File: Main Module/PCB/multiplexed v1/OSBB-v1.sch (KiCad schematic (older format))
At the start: 30 parts, among them P1 AUX 1, P10 +3.3V Pins, P11 BTN-1-4, P12 BTN-5-8, P13 BTN-9-12, P14 EXTRA Pins, P15 BTN-17-20, P16 BTN-13-16, P17 BTN-25-28, P18 BTN-21-24, P19 BTN-29-32, P2 AUX 2, P3 AUX 3, P4 Pit limiter, P5 Rotary Encoders, P6 GND Pins, Q1 Q_NPN_CBE, Q2 Q_NPN_CBE, Q3 Q_NPN_CBE, U1 74HC4051, U2 74HC4051, U3 74HC4051, U4 74HC4051, U5 Teensy3.2

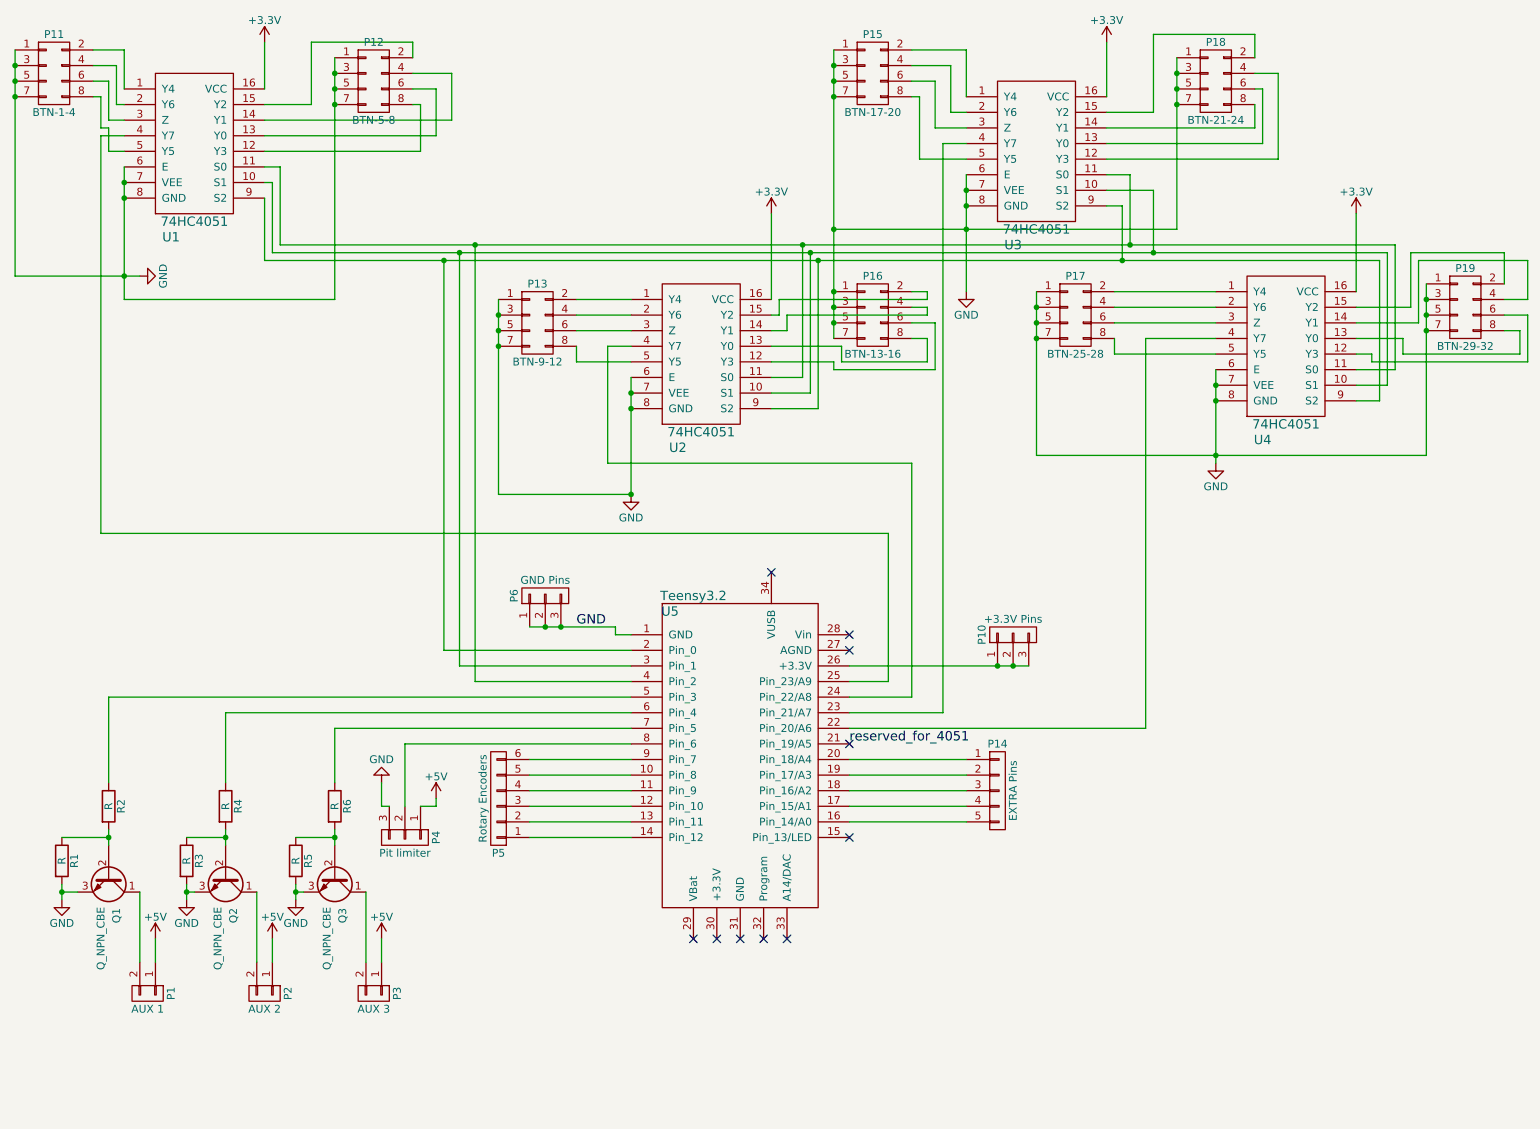
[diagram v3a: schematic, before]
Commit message: * updated schematic to use 2x32 pin header to make it easier to connect PCB * PCB is connected, still needs to be checked
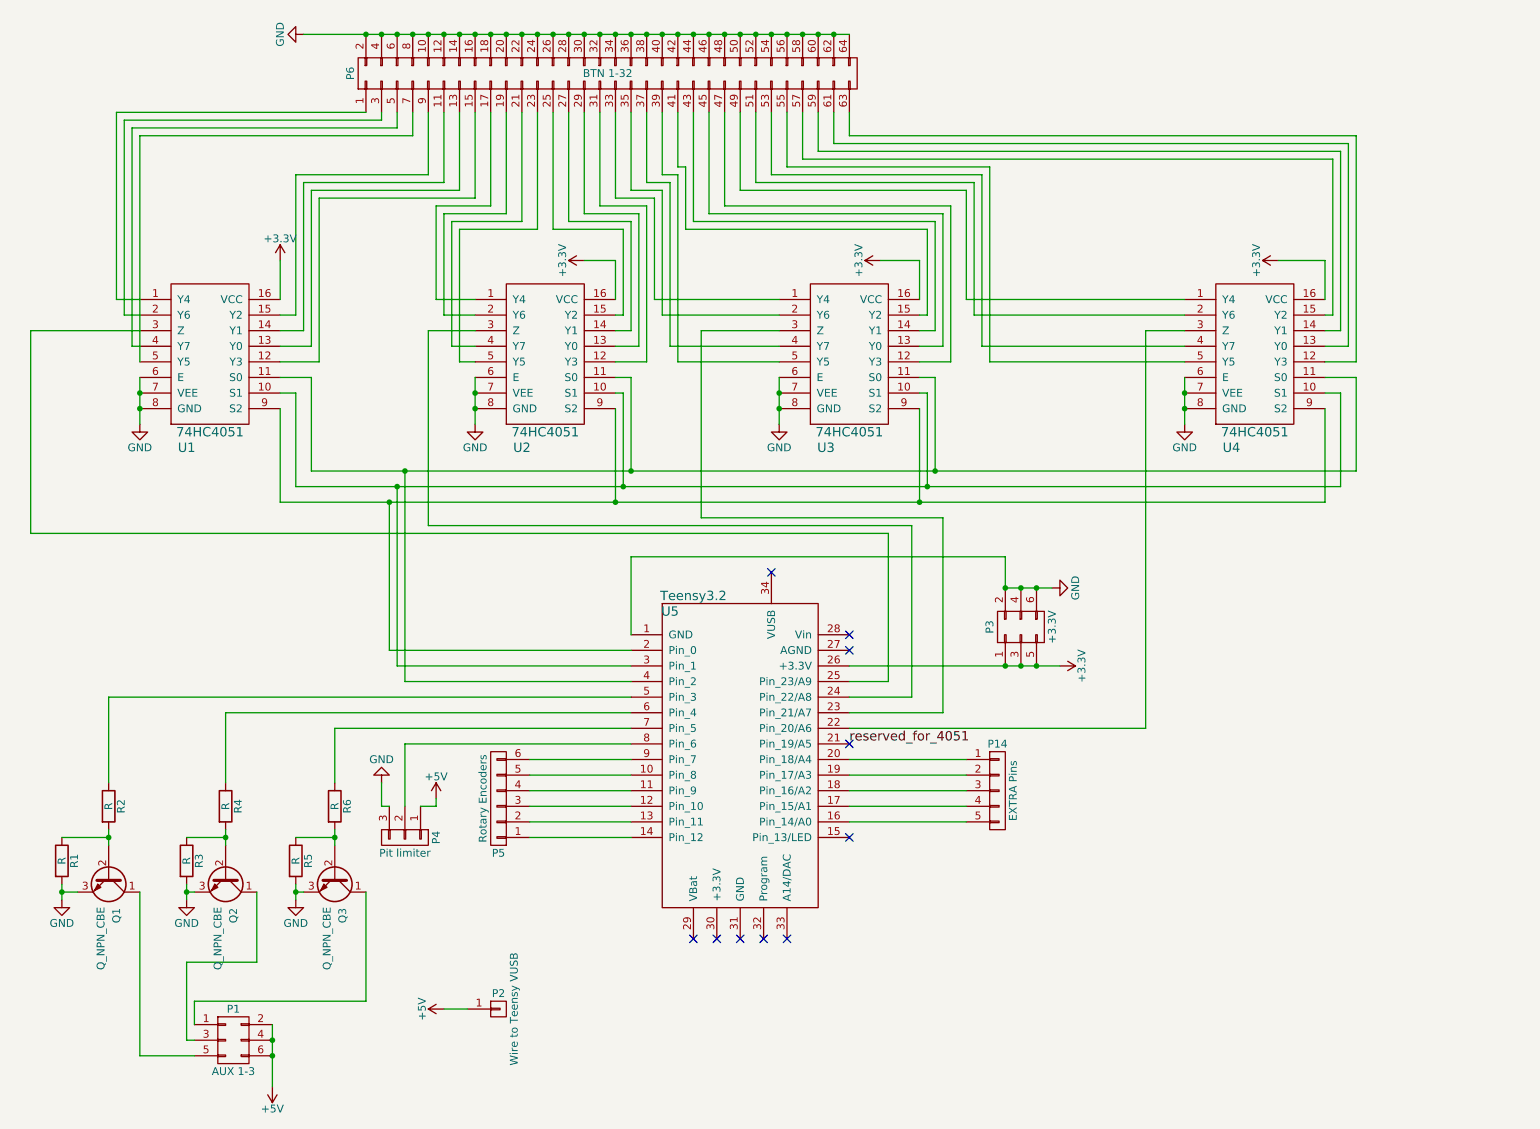
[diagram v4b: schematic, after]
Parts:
- removed P1: AUX 1, Pin_Headers:Pin_Header_Angled_1x02, symbol CONN_01X02
- removed P10: +3.3V Pins, Pin_Headers:Pin_Header_Angled_1x03, symbol CONN_01X03
- removed P11: BTN-1-4, Pin_Headers:Pin_Header_Angled_2x04, symbol CONN_02X04
- removed P12: BTN-5-8, Pin_Headers:Pin_Header_Angled_2x04, symbol CONN_02X04
- removed P13: BTN-9-12, Pin_Headers:Pin_Header_Angled_2x04, symbol CONN_02X04
- removed P15: BTN-17-20, Pin_Headers:Pin_Header_Angled_2x04, symbol CONN_02X04
- removed P16: BTN-13-16, Pin_Headers:Pin_Header_Angled_2x04, symbol CONN_02X04
- removed P17: BTN-25-28, Pin_Headers:Pin_Header_Angled_2x04, symbol CONN_02X04
- removed P18: BTN-21-24, Pin_Headers:Pin_Header_Angled_2x04, symbol CONN_02X04
- removed P19: BTN-29-32, Pin_Headers:Pin_Header_Angled_2x04, symbol CONN_02X04
- removed P2: AUX 2, Pin_Headers:Pin_Header_Angled_1x02, symbol CONN_01X02
- removed P3: AUX 3, Pin_Headers:Pin_Header_Angled_1x02, symbol CONN_01X02
- removed P6: GND Pins, Pin_Headers:Pin_Header_Angled_1x03, symbol CONN_01X03
- added P1: AUX 1-3, Pin_Headers:Pin_Header_Angled_2x03, symbol CONN_02X03
- added P2: Wire to Teensy VUSB, Pin_Headers:Pin_Header_Straight_1x01, symbol CONN_01X01
- added P3: +3.3V, Pin_Headers:Pin_Header_Angled_2x03, symbol CONN_02X03
- added P6: BTN 1-32, Pin_Headers:Pin_Header_Angled_2x32, symbol CONN_02X32
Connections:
- net +3V3: now also U5.26 (+3.3V), P3.1 (P1), P3.3 (P3), P3.5 (P5)
- net +5V: now also P1.2 (P2), P1.4 (P4), P1.6 (P6), P2.1 (P1)
- net GND: now also P3.2 (P2), P3.4 (P4), P3.6 (P6), P6.10 (P10), P6.12 (P12), P6.14 (P14), P6.16 (P16), P6.18 (P18), P6.2 (P2), P6.20 (P20), P6.22 (P22), P6.24 (P24), P6.26 (P26), P6.28 (P28), P6.30 (P30), P6.32 (P32), P6.34 (P34), P6.36 (P36), P6.38 (P38), P6.4 (P4), P6.40 (P40), P6.42 (P42), P6.44 (P44), P6.46 (P46), P6.48 (P48), P6.50 (P50), P6.52 (P52), P6.54 (P54), P6.56 (P56), P6.58 (P58), P6.6 (P6), P6.60 (P60), P6.62 (P62), P6.64 (P64), P6.8 (P8)
- net at U2.1 (Y4): now also P6.17 (P17)
- net at U2.12 (Y3): now also P6.31 (P31)
- net at U2.13 (Y0): now also P6.29 (P29)
- net at U2.14 (Y1): now also P6.27 (P27)
- net at U2.15 (Y2): now also P6.25 (P25)
- net at U2.2 (Y6): now also P6.19 (P19)
- net at U2.3 (Z): now also U5.24 (Pin_22/A8)
- net at U2.4 (Y7): now also P6.21 (P21); no longer U5.24 (Pin_22/A8)
- net at U2.5 (Y5): now also P6.23 (P23)
- net at U3.1 (Y4): now also P6.33 (P33)
- net at U3.12 (Y3): now also P6.47 (P47)
- net at U3.13 (Y0): now also P6.45 (P45)
- net at U3.14 (Y1): now also P6.43 (P43)
- net at U3.15 (Y2): now also P6.41 (P41)
- net at U3.2 (Y6): now also P6.35 (P35)
- net at U3.3 (Z): now also U5.23 (Pin_21/A7)
- net at U3.4 (Y7): now also P6.37 (P37); no longer U5.23 (Pin_21/A7)
- net at U3.5 (Y5): now also P6.39 (P39)
- net at U1.1 (Y4): now also P6.1 (P1)
- net at U1.12 (Y3): now also P6.15 (P15)
- net at U1.13 (Y0): now also P6.13 (P13)
- net at U1.14 (Y1): now also P6.11 (P11)
- net at U1.15 (Y2): now also P6.9 (P9)
- net at U1.2 (Y6): now also P6.3 (P3)
- net at U1.3 (Z): now also U5.25 (Pin_23/A9)
- net at U1.4 (Y7): now also P6.5 (P5); no longer U5.25 (Pin_23/A9)
- net at U1.5 (Y5): now also P6.7 (P7)
- net at U4.1 (Y4): now also P6.49 (P49)
- net at U4.12 (Y3): now also P6.63 (P63)
- net at U4.13 (Y0): now also P6.61 (P61)
- net at U4.14 (Y1): now also P6.59 (P59)
- net at U4.15 (Y2): now also P6.57 (P57)
- net at U4.2 (Y6): now also P6.51 (P51)
- net at U4.3 (Z): now also U5.22 (Pin_20/A6)
- net at U4.4 (Y7): now also P6.53 (P53); no longer U5.22 (Pin_20/A6)
- net at U4.5 (Y5): now also P6.55 (P55)
- net at Q1.1 (C): now also P1.5 (P5)
- net at Q2.1 (C): now also P1.3 (P3)
- net at Q3.1 (C): now also P1.1 (P1)
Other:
- moved on the sheet: U1, U2, U3, U4
